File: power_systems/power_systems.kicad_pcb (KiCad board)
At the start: 2 copper layers, 75.7 x 39.9 mm, 13 parts, among them J1 Screw_Terminal_01x02, J2 Screw_Terminal_01x02, J3 Screw_Terminal_01x02, U1 LM2576HVS-5, U2 LM2576HVS-12

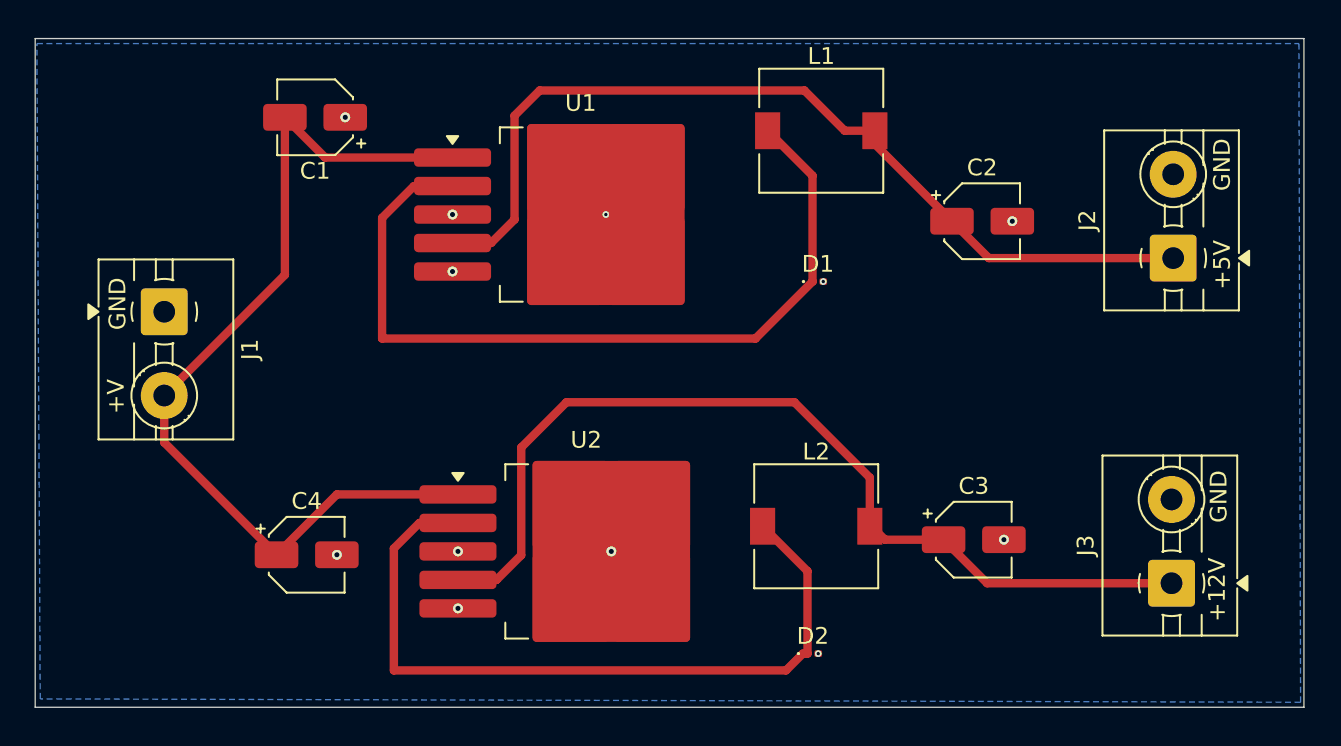
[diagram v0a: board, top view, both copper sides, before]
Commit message: PCB Fixes
Working on determining if Schottky needs to be through hole or not, standby.
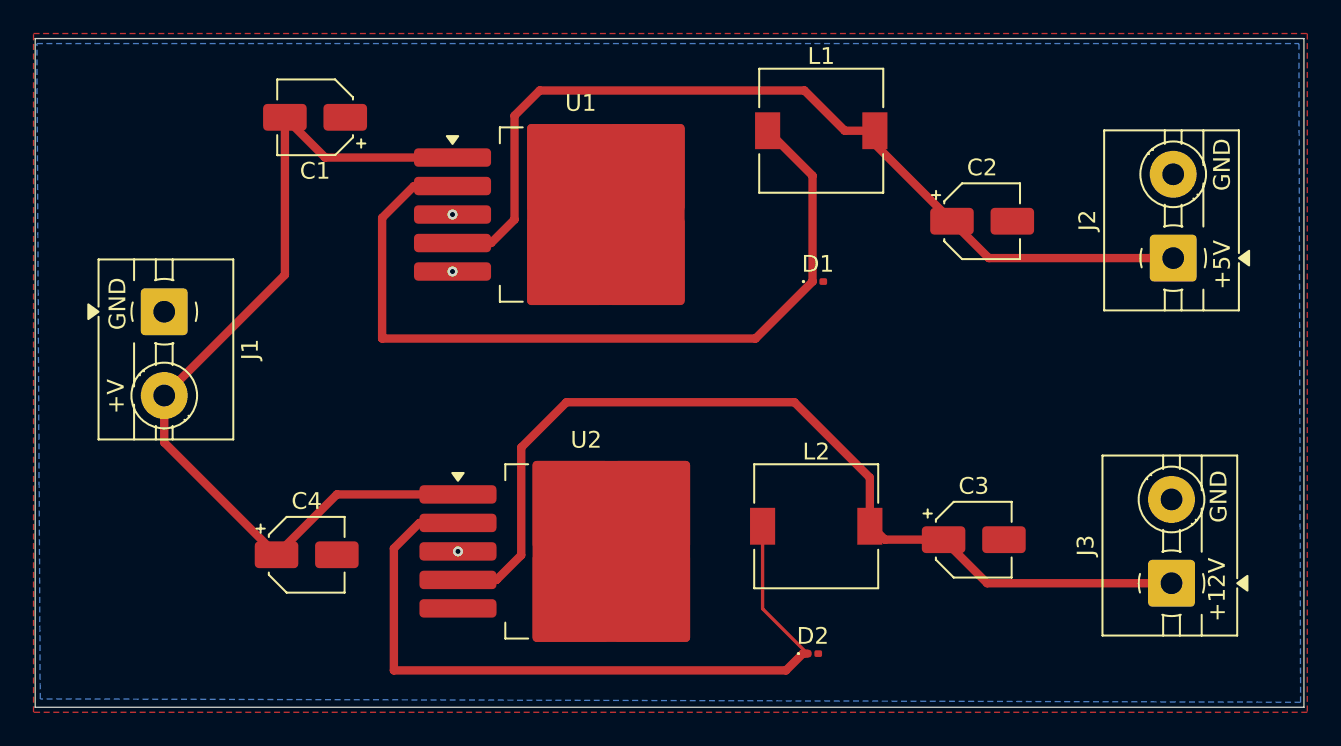
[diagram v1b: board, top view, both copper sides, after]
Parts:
- C3: value C -> 1000uF
- L2: value L -> 100uH
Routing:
- net GND: vias 12 -> 3
- added copper zone on F.Cu, net GND
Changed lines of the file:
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@@
 		(property ki_fp_filters "TerminalBlock*:*")
 		(sheetname "/")
-		(sheetfile "buck_converter.kicad_sch")
+		(sheetfile "power_systems.kicad_sch")
 		(attr through_hole)
 		(fp_line
@@
 		(property ki_fp_filters "C_*")
 		(sheetname "/")
-		(sheetfile "buck_converter.kicad_sch")
+		(sheetfile "power_systems.kicad_sch")
 		(attr smd)
 		(fp_line
@@
 		(property ki_fp_filters "TerminalBlock*:*")
 		(sheetname "/")
-		(sheetfile "buck_converter.kicad_sch")
+		(sheetfile "power_systems.kicad_sch")
 		(attr through_hole)
 		(fp_line
@@
 			)
 		)
-		(property "Value" "C"
+		(property "Value" "1000uF"
 			(at 0 3.2 0)
 			(layer "F.Fab")
@@
 		(property ki_fp_filters "C_*")
 		(sheetname "/")
-		(sheetfile "buck_converter.kicad_sch")
+		(sheetfile "power_systems.kicad_sch")
 		(attr smd)
 		(fp_line
@@
 		(property ki_fp_filters "C_*")
 		(sheetname "/")
-		(sheetfile "buck_converter.kicad_sch")
+		(sheetfile "power_systems.kicad_sch")
 		(attr smd)
 		(fp_line
@@
 		(property ki_fp_filters "TO?263*")
 		(sheetname "/")
-		(sheetfile "buck_converter.kicad_sch")
+		(sheetfile "power_systems.kicad_sch")
 		(attr smd)
 		(fp_line
@@
 		(property ki_fp_filters "C_*")
 		(sheetname "/")
-		(sheetfile "buck_converter.kicad_sch")
+		(sheetfile "power_systems.kicad_sch")
 		(attr smd)
 		(fp_line
@@
 		(property ki_fp_filters "TO-???* *_Diode_* *SingleDiode* D_*")
 		(sheetname "/")
-		(sheetfile "buck_converter.kicad_sch")
+		(sheetfile "power_systems.kicad_sch")
 		(attr smd)
 		(fp_circle
@@
 		(property ki_fp_filters "TO?263*")
 		(sheetname "/")
-		(sheetfile "buck_converter.kicad_sch")
+		(sheetfile "power_systems.kicad_sch")
 		(attr smd)
 		(fp_line
@@
 		(property ki_fp_filters "Choke_* *Coil* Inductor_* L_*")
 		(sheetname "/")
-		(sheetfile "buck_converter.kicad_sch")
+		(sheetfile "power_systems.kicad_sch")
 		(attr smd)
 		(fp_line
@@
 			)
 		)
-		(property "Value" "L"
+		(property "Value" "100uH"
 			(at 0 4.45 0)
 			(layer "F.Fab")
@@
 		(property ki_fp_filters "Choke_* *Coil* Inductor_* L_*")
 		(sheetname "/")
-		(sheetfile "buck_converter.kicad_sch")
+		(sheetfile "power_systems.kicad_sch")
 		(attr smd)
 		(fp_line
@@
 		(property ki_fp_filters "TerminalBlock*:*")
 		(sheetname "/")
-		(sheetfile "buck_converter.kicad_sch")
+		(sheetfile "power_systems.kicad_sch")
 		(attr through_hole)
 		(fp_line
@@
 		(property ki_fp_filters "TO-???* *_Diode_* *SingleDiode* D_*")
 		(sheetname "/")
-		(sheetfile "buck_converter.kicad_sch")
+		(sheetfile "power_systems.kicad_sch")
 		(attr smd)
 		(fp_circle
@@
 	)
 	(via
-		(at 79.9 66.2)
-		(size 0.6)
-		(drill 0.3)
-		(layers "F.Cu" "B.Cu")
-		(net 2)
-	)
-	(via
-		(at 69.12 50.8)
-		(size 0.4)
-		(drill 0.2)
-		(layers "F.Cu" "B.Cu")
-		(net 2)
-	)
-	(via
-		(at 47.325 70.3)
-		(size 0.6)
-		(drill 0.3)
-		(layers "F.Cu" "B.Cu")
-		(net 2)
-	)
-	(via
-		(at 40.1 67.1)
-		(size 0.6)
-		(drill 0.3)
-		(layers "F.Cu" "B.Cu")
-		(net 2)
-	)
-	(via
 		(at 47 46.8)
 		(size 0.6)
@@
 	)
 	(via
-		(at 56.15 46.8)
-		(size 0.4)
-		(drill 0.2)
-		(layers "F.Cu" "B.Cu")
-		(net 2)
-	)
-	(via
-		(at 80.4 47.2)
-		(size 0.6)
-		(drill 0.3)
-		(layers "F.Cu" "B.Cu")
-		(net 2)
-	)
-	(via
-		(at 68.82 73)
-		(size 0.4)
-		(drill 0.2)
-		(layers "F.Cu" "B.Cu")
-		(net 2)
-	)
-	(via
-		(at 56.475 66.9)
-		(size 0.6)
-		(drill 0.3)
-		(layers "F.Cu" "B.Cu")
-		(net 2)
-	)
-	(via
 		(at 47 50.2)
 		(size 0.6)
@@
 		(net 2)
 	)
-	(via
-		(at 40.6 41)
-		(size 0.6)
-		(drill 0.3)
-		(layers "F.Cu" "B.Cu")
-		(net 2)
-	)
 	(segment
 		(start 47 48.5)
@@
 	)
 	(segment
+		(start 65.5 70.32)
+		(end 68.18 73)
+		(width 0.2)
+		(layer "F.Cu")
+		(net 6)
+	)
+	(segment
 		(start 47.325 65.2)
 		(end 45.025 65.2)
@@
 	)
 	(segment
-		(start 68.18 68.08)
-		(end 65.5 65.4)
-		(width 0.5)
+		(start 65.5 65.4)
+		(end 65.5 70.32)
+		(width 0.2)
 		(layer "F.Cu")
 		(net 6)
@@
 	)
 	(segment
-		(start 68.18 73)
-		(end 68.18 68.08)
-		(width 0.5)
-		(layer "F.Cu")
-		(net 6)
-	)
-	(segment
 		(start 43.5 74)
 		(end 66.9 74)
@@
 	)
 	(zone
+		(net 2)
+		(net_name "GND")
+		(layer "F.Cu")
+		(hatch edge 0.5)
+		(priority 1)
+		(connect_pads
+			(clearance 0.5)
+		)
+		(min_thickness 0.25)
+		(filled_areas_thickness no)
+		(fill yes
+			(thermal_gap 0.5)
+			(thermal_bridge_width 0.5)
+		)
+		(polygon
+			(pts
+				(xy 22 36) (xy 98 36) (xy 98 76.5) (xy 22 76.5)
+			)
+		)
+	)
+	(zone

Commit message: Fixed DRC Errors.
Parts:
- C3: value 1000uF -> C
- L2: value 100uH -> L
